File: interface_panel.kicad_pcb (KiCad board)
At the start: 2 copper layers, 48.5 x 32 mm, 7 parts, among them J1 Conn_02x04_Odd_Even

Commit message: panel_final
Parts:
- added REF**: MountingHole_2.2mm_M2_DIN965_Pad, MountingHole:MountingHole_2.2mm_M2_DIN965_Pad, F.Cu at (166.2, 64.0)
- added REF**: MountingHole_2.2mm_M2_DIN965_Pad, MountingHole:MountingHole_2.2mm_M2_DIN965_Pad, F.Cu at (125.2, 63.6)
- added REF**: MountingHole_2.2mm_M2_DIN965_Pad, MountingHole:MountingHole_2.2mm_M2_DIN965_Pad, F.Cu at (166.0, 86.8)
- added REF**: MountingHole_2.2mm_M2_DIN965_Pad, MountingHole:MountingHole_2.2mm_M2_DIN965_Pad, F.Cu at (125.2, 86.8)
- R1: footprint Resistor_THT:R_Axial_DIN0207_L6.3mm_D2.5mm_P7.62mm_Horizontal -> Resistor_THT:R_Axial_DIN0204_L3.6mm_D1.6mm_P5.08mm_Horizontal
- moved H-1 3.40 mm to (137.6, 86.3)
- moved D1 3.14 mm to (163.0, 80.6)
- moved R1 2.20 mm to (165.2, 76.5)
- moved oled1 1.81 mm to (161.8, 78.3)
- moved ON/OFF 1.43 mm to (148.1, 86.3)
- moved H-2 0.55 mm to (158.7, 86.3)
- renumbered 0/1 to ON/OFF
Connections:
- J1 pad 3: BT-2 -> BT-Pwr
- J1 pad 5: BT-Pwr -> BT-1
- J1 pad 7: BT-1 -> BT-2
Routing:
- net BT-2: track 12.5 -> 28.3 mm, vias 0 -> 1
- net BT-1: track 12.3 -> 24.2 mm
- net BT-Pwr: track 10.8 -> 18.7 mm
- net Net-(D1-A): track 9.71 -> 4.26 mm
- net S. LED: track 21.0 -> 22.6 mm
- net SCL: track 15.0 -> 16.0 mm
- net SDA: track 18.4 -> 19.4 mm
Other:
- board size 48.5 x 32 mm -> 47.1 x 29.7 mm

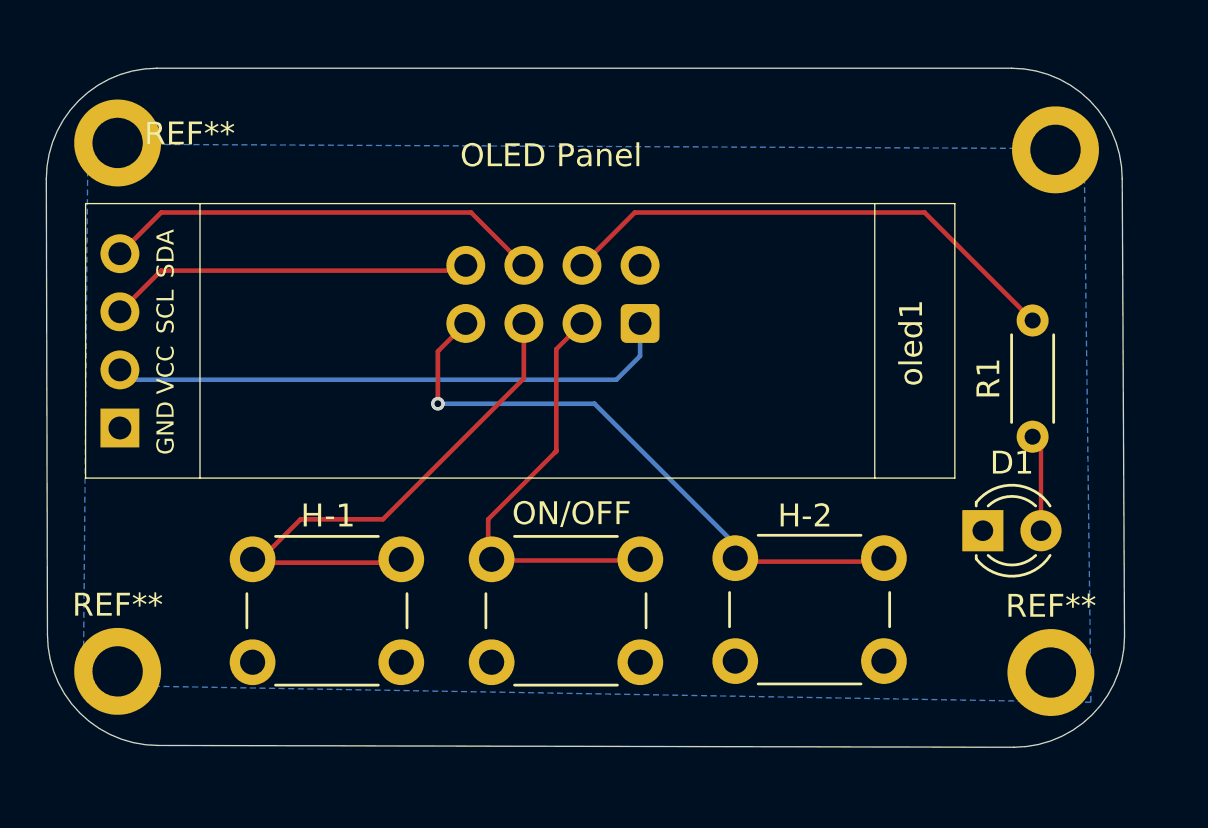
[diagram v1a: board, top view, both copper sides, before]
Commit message: round tracks
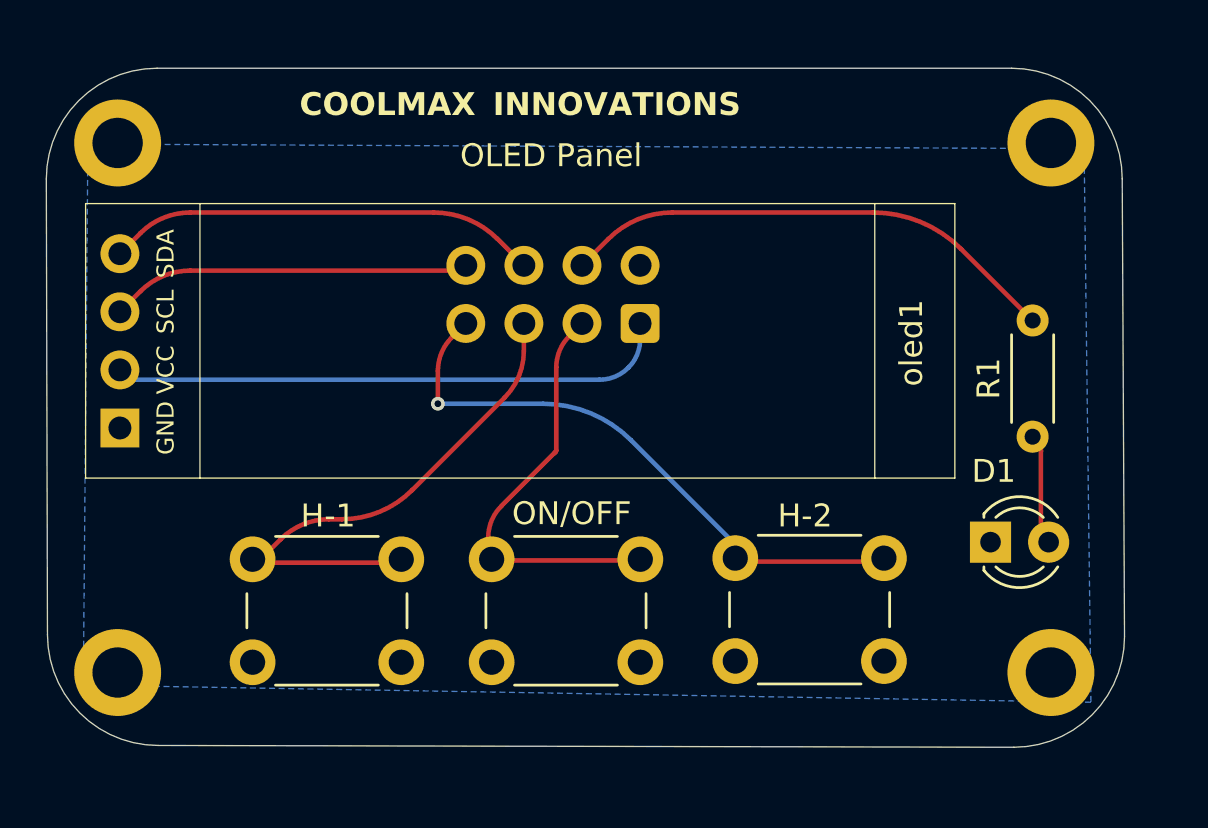
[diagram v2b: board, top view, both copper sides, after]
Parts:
- added REF**: Innov-0.3thck-1-1, Logo:Innov-0.3thck-1-1, F.Cu at (151.6, 62.5)
- added REF**: Coolmax-Logo, Logo:Coolmax-Logo, F.Cu at (161.1, 63.2)
- moved D1 0.60 mm to (163.4, 81.1)
- moved REF** 0.36 mm to (166.0, 63.6)
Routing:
- net BT-2: track 28.3 -> 27.5 mm
- net BT-1: track 24.2 -> 23.5 mm
- net Net-(D1-A): track 4.26 -> 4.87 mm

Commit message: adjusted layout with bom & gerber files
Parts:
- moved oled1 1.30 mm to (163.1, 78.2)
- moved R1 1.15 mm to (166.3, 76.4)
- moved D1 0.30 mm to (163.3, 81.4)
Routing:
- net S. LED: track 22.2 -> 24.5 mm
- net 5V: track 25.1 -> 23.5 mm
- net SCL: track 15.8 -> 14.6 mm
- net Net-(D1-A): track 4.87 -> 5.90 mm
- net SDA: track 19.0 -> 18.0 mm
- net BT-2: track 27.5 -> 28.3 mm
- net BT-1: track 23.5 -> 24.2 mm
